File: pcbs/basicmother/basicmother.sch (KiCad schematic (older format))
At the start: 10 parts

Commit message: Primera version de la placa madre y sigo agregando bibliotecas
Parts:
- added C? (x2): 22n, symbol CPSMALL
- added C? (x2): 100n, symbol CPSMALL
- added C? (x2): 100uA, symbol CAPAPOL
- added P?: CONN_3X2, symbol CONN_3X2
- added U?: PTN4050, symbol PTN4050
- added X?: 18.452 MHz, symbol CRYSTAL
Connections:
- net labels added: MISO, MOSI, RST, SCK
- wire segments 66 -> 112
- no-connect marks 27 -> 30
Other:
- note added: "Bajar de 14.8 a 5"
- note added: "Dejando abierto el \npin 3 la salida es 5 V"
- note added: "Elevar de 5 a 12 con PTN04050c"

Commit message: Actualizando la nueva placa base, falta el amplificador para el parlante
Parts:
- removed C? (x2): 22n, symbol CPSMALL
- removed C? (x2): 100n, symbol CPSMALL
- removed C? (x2): 100uA, symbol CAPAPOL
- removed P?: CONN_8, symbol CONN_8
- removed P?: CONN_5X2, symbol CONN_5X2
- removed P? (x4): CONN_2, symbol CONN_2
- removed P?: CONN_3X2, symbol CONN_3X2
- removed U?: PTN4050, symbol PTN4050
- added C? (x2): 22n, symbol Csmall
- added C? (x2): 100n, symbol Csmall
- added P?: CONN_02X03, symbol CONN_02X03
- added P?: CONN_02X05, symbol CONN_02X05
- added P? (x2): CONN_01X02, symbol CONN_01X02
- added P?: CONN_01X08, symbol CONN_01X08
- X?: value 18.452 MHz -> 18.432 MHz
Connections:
- net labels added: +15V
- net labels removed: BAT, POWER
- wire segments 112 -> 114
- no-connect marks 30 -> 28
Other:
- note added: "Comunicacion con el control remoto"
- note added: "Conector para los ojos"
- note added: "Control de los ojos"
- note removed: "Bajar de 14.8 a 5"
- note removed: "CONECTOR DE BATERIA"
- note removed: "CONECTOR DE ENCENDIDO"
- note removed: "Dejando abierto el \npin 3 la salida es 5 V"
- note removed: "Elevar de 5 a 12 con PTN04050c"
- moved on the sheet: IC?, P?, U?, X?

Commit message: actualizo la placa principal
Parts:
- removed P?: CONN_01X08, symbol CONN_01X08
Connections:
- net labels added: Audio
- wire segments 114 -> 123
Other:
- note removed: "CONTRO DE PUENTE H"
- moved on the sheet: P?
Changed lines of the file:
@@
 LIBS:ptn04050c
 LIBS:ptn78000w
+LIBS:drv8432
 LIBS:basicmother-cache
 EELAYER 25 0
@@
 $Descr A4 11693 8268
 encoding utf-8
-Sheet 1 2
+Sheet 1 4
 Title ""
 Date "11 jan 2014"
@@
 Comment4 ""
 $EndDescr
-Text Label 9350 5500 2    60   ~ 0
+Text Label 8000 5700 0    60   ~ 0
 /RESET_CD
-Text Label 9350 5600 2    60   ~ 0
+Text Label 8000 5150 0    60   ~ 0
 PWM_C
-Text Label 9350 5700 2    60   ~ 0
+Text Label 8000 5000 0    60   ~ 0
 PWM_B
-Text Label 9350 5800 2    60   ~ 0
+Text Label 8000 5550 0    60   ~ 0
 /RESET_AB
-Text Label 9350 5900 2    60   ~ 0
+Text Label 8000 4850 0    60   ~ 0
 PWM_A
-Text Label 9350 6000 2    60   ~ 0
+Text Label 8000 5850 0    60   ~ 0
 /FAULT
-Text Label 9350 6100 2    60   ~ 0
+Text Label 8000 6000 0    60   ~ 0
 /OTW
-Text Label 9350 5400 2    60   ~ 0
+Text Label 8000 5300 0    60   ~ 0
 PWM_D
 $Comp
@@
 	3300 5050 3300 4700
 Wire Wire Line
-	1050 5400 1450 5400
+	1050 5400 1200 5400
+Wire Wire Line
+	1200 5400 1450 5400
 $Comp
 L GND #PWR?
@@
 	1000 850  1000 2050
 Wire Notes Line
-	8400 6250 9600 6250
-Wire Notes Line
-	9600 5050 8400 5050
-Wire Notes Line
-	8400 5050 8400 6250
-Wire Notes Line
 	4400 4450 4400 5750
 Wire Notes Line
@@
 Text Notes 1700 1000 0    60   ~ 0
 DIPSWITCH
-Text Notes 9100 5200 0    60   ~ 0
-CONTRO DE PUENTE H
-Wire Notes Line
-	9850 5050 10850 5050
-Wire Notes Line
-	10850 5050 10850 6250
-Wire Notes Line
-	10850 6250 9850 6250
-Wire Wire Line
-	10550 5650 10550 5500
-Wire Wire Line
-	10550 5500 10400 5500
-$Comp
-L GND #PWR?
-U 1 1 52D08C4C
-P 10400 5500
-F 0 "#PWR?" H 10400 5500 30  0001 C CNN
-F 1 "GND" H 10400 5430 30  0001 C CNN
-F 2 "" H 10400 5500 60  0000 C CNN
-F 3 "" H 10400 5500 60  0000 C CNN
-	1    10400 5500
-	0    1    1    0
-$EndComp
-Wire Wire Line
-	10650 5650 10650 5500
-Wire Wire Line
-	10650 5500 10800 5500
-Wire Notes Line
-	9550 5050 9950 5050
-Wire Notes Line
-	9550 6250 10100 6250
-Wire Wire Line
-	9850 5650 9850 5500
-Wire Wire Line
-	9850 5500 9700 5500
-$Comp
-L GND #PWR?
-U 1 1 52D08D21
-P 9700 5500
-F 0 "#PWR?" H 9700 5500 30  0001 C CNN
-F 1 "GND" H 9700 5430 30  0001 C CNN
-F 2 "" H 9700 5500 60  0000 C CNN
-F 3 "" H 9700 5500 60  0000 C CNN
-	1    9700 5500
-	0    1    1    0
-$EndComp
-Wire Wire Line
-	9950 5650 9950 5500
-Wire Wire Line
-	9950 5500 10100 5500
 $Comp
 L +12V #PWR?
 U 1 1 52D08D2C
-P 10100 5450
-F 0 "#PWR?" H 10100 5400 20  0001 C CNN
-F 1 "+12V" H 10100 5550 30  0000 C CNN
-F 2 "" H 10100 5450 60  0000 C CNN
-F 3 "" H 10100 5450 60  0000 C CNN
-	1    10100 5450
+P 10150 4800
+F 0 "#PWR?" H 10150 4750 20  0001 C CNN
+F 1 "+12V" H 10150 4900 30  0000 C CNN
+F 2 "" H 10150 4800 60  0000 C CNN
+F 3 "" H 10150 4800 60  0000 C CNN
+	1    10150 4800
 	1    0    0    -1
 $EndComp
@@
 $EndComp
 Wire Wire Line
-	7000 1950 7150 1950
+	7000 1950 7050 1950
+Wire Wire Line
+	7050 1950 7150 1950
 Wire Wire Line
 	7000 1950 7000 1900
@@
 	7750 1950 7850 1950
 Wire Wire Line
-	7850 1800 7850 2000
+	7850 1800 7850 1950
+Wire Wire Line
+	7850 1950 7850 2000
 Wire Wire Line
 	7850 1800 6700 1800
@@
 	4750 1150 4750 1200
 Wire Wire Line
-	4550 1200 4800 1200
+	4550 1200 4750 1200
+Wire Wire Line
+	4750 1200 4800 1200
 $Comp
 L +5V #PWR?
@@
 	4800 3400 4700 3400
 Wire Wire Line
-	4700 3400 4700 3600
+	4700 3400 4700 3500
+Wire Wire Line
+	4700 3500 4700 3600
 Wire Wire Line
 	4800 3500 4700 3500
@@
 L CONN_01X02 P?
 U 1 1 54D56E87
-P 10600 5850
-F 0 "P?" H 10600 6000 50  0000 C CNN
-F 1 "CONN_01X02" V 10700 5850 50  0000 C CNN
-F 2 "" H 10600 5850 60  0000 C CNN
-F 3 "" H 10600 5850 60  0000 C CNN
-	1    10600 5850
-	0    1    1    0
+P 10350 5550
+F 0 "P?" H 10350 5700 50  0000 C CNN
+F 1 "CONN_01X02" V 10450 5550 50  0000 C CNN
+F 2 "" H 10350 5550 60  0000 C CNN
+F 3 "" H 10350 5550 60  0000 C CNN
+	1    10350 5550
+	1    0    0    -1
 $EndComp
 $Comp
 L CONN_01X02 P?
 U 1 1 54D57006
-P 9900 5850
-F 0 "P?" H 9900 6000 50  0000 C CNN
-F 1 "CONN_01X02" V 10000 5850 50  0000 C CNN
-F 2 "" H 9900 5850 60  0000 C CNN
-F 3 "" H 9900 5850 60  0000 C CNN
-	1    9900 5850
-	0    1    1    0
-$EndComp
-$Comp
-L CONN_01X08 P?
-U 1 1 54D5705C
-P 8600 5750
-F 0 "P?" H 8600 6200 50  0000 C CNN
-F 1 "CONN_01X08" V 8700 5750 50  0000 C CNN
-F 2 "" H 8600 5750 60  0000 C CNN
-F 3 "" H 8600 5750 60  0000 C CNN
-	1    8600 5750
-	-1   0    0    -1
-$EndComp
-Wire Wire Line
-	9350 6100 8800 6100
-Wire Wire Line
-	8800 6000 9350 6000
-Wire Wire Line
-	9350 5900 8800 5900
-Wire Wire Line
-	8800 5800 9350 5800
-Wire Wire Line
-	9350 5700 8800 5700
-Wire Wire Line
-	8800 5600 9350 5600
-Wire Wire Line
-	9350 5500 8800 5500
-Wire Wire Line
-	8800 5400 9350 5400
+P 10350 5250
+F 0 "P?" H 10350 5400 50  0000 C CNN
+F 1 "CONN_01X02" V 10450 5250 50  0000 C CNN
+F 2 "" H 10350 5250 60  0000 C CNN
+F 3 "" H 10350 5250 60  0000 C CNN
+	1    10350 5250
+	1    0    0    -1
+$EndComp
+Wire Wire Line
+	8000 6000 8550 6000
+Wire Wire Line
+	8550 5850 8000 5850
+Wire Wire Line
+	8000 4850 8550 4850
+Wire Wire Line
+	8550 5550 8000 5550
+Wire Wire Line
+	8000 5000 8550 5000
+Wire Wire Line
+	8550 5150 8000 5150
+Wire Wire Line
+	8000 5700 8550 5700
+Wire Wire Line
+	8550 5300 8000 5300
 $Sheet
 S 10200 950  750  1000
@@
 L +15V #PWR?
 U 1 1 54D5DC54
-P 10800 5450
-F 0 "#PWR?" H 10800 5300 60  0001 C CNN
-F 1 "+15V" H 10800 5590 60  0000 C CNN
-F 2 "" H 10800 5450 60  0000 C CNN
-F 3 "" H 10800 5450 60  0000 C CNN
-	1    10800 5450
-	1    0    0    -1
-$EndComp
-Wire Wire Line
-	10800 5500 10800 5450
-Wire Wire Line
-	10100 5500 10100 5450
+P 9950 4700
+F 0 "#PWR?" H 9950 4550 60  0001 C CNN
+F 1 "+15V" H 9950 4840 60  0000 C CNN
+F 2 "" H 9950 4700 60  0000 C CNN
+F 3 "" H 9950 4700 60  0000 C CNN
+	1    9950 4700
+	1    0    0    -1
+$EndComp
+$Comp
+L +15V #PWR?
+U 1 1 54DE957E
+P 9750 900
+F 0 "#PWR?" H 9750 750 60  0001 C CNN
+F 1 "+15V" H 9750 1040 60  0000 C CNN
+F 2 "" H 9750 900 60  0000 C CNN
+F 3 "" H 9750 900 60  0000 C CNN
+	1    9750 900
+	1    0    0    -1
+$EndComp
+$Sheet
+S 9500 2500 1100 950
+U 54DEA09E
+F0 "sound" 60
+F1 "sound.sch" 60
+F2 "In" I L 9500 3000 60
+F3 "5V" I L 9500 2700 60
+F4 "GND" I L 9500 3250 60
+$EndSheet
+Wire Wire Line
+	9500 2700 9300 2700
+Wire Wire Line
+	9300 2700 9300 2300
+$Comp
+L +5V #PWR?
+U 1 1 54DEDB40
+P 9300 2300
+F 0 "#PWR?" H 9300 2390 20  0001 C CNN
+F 1 "+5V" H 9300 2390 30  0000 C CNN
+F 2 "" H 9300 2300 60  0000 C CNN
+F 3 "" H 9300 2300 60  0000 C CNN
+	1    9300 2300
+	1    0    0    -1
+$EndComp
+$Comp
+L GND #PWR?
+U 1 1 54DEDBE5
+P 9300 3350
+F 0 "#PWR?" H 9300 3350 30  0001 C CNN
+F 1 "GND" H 9300 3280 30  0001 C CNN
+F 2 "" H 9300 3350 60  0000 C CNN
+F 3 "" H 9300 3350 60  0000 C CNN
+	1    9300 3350
+	1    0    0    -1
+$EndComp
+Wire Wire Line
+	9300 3350 9300 3250
+Wire Wire Line
+	9300 3250 9500 3250
+Wire Wire Line
+	9500 3000 9150 3000
+Text Label 9150 3000 0    60   ~ 0
+Audio
+Text Label 3750 7300 2    60   ~ 0
+Audio
+Wire Wire Line
+	3750 7300 3300 7300
+$Sheet
+S 8550 4700 1250 1450
+U 54DEEEE7
+F0 "motordrv" 60
+F1 "motordrv.sch" 60
+F2 "MOUT_D" U R 9800 5600 60
+F3 "MOUT_C" U R 9800 5500 60
+F4 "MOUT_B" U R 9800 5300 60
+F5 "MOUT_A" U R 9800 5200 60
+F6 "~RESET_AB" I L 8550 5550 60
+F7 "~RESET_CD" I L 8550 5700 60
+F8 "PWM_D" I L 8550 5300 60
+F9 "PWM_C" I L 8550 5150 60
+F10 "PWM_B" I L 8550 5000 60
+F11 "PWM_A" I L 8550 4850 60
+F12 "PVDD" I R 9800 4850 60
+F13 "~FAULT" O L 8550 5850 60
+F14 "~OTW" O L 8550 6000 60
+F15 "DGND" I R 9800 5850 60
+F16 "DVDD" I R 9800 5000 60
+$EndSheet
+Wire Wire Line
+	9950 4700 9950 4850
+Wire Wire Line
+	9950 4850 9800 4850
+Wire Wire Line
+	10150 4800 10150 5000
+Wire Wire Line
+	10150 5000 9800 5000
+Wire Wire Line
+	10150 5500 9800 5500
+Wire Wire Line
+	9800 5600 10150 5600
+Wire Wire Line
+	10150 5300 9800 5300
+Wire Wire Line
+	9800 5200 10150 5200
 $EndSCHEMATC

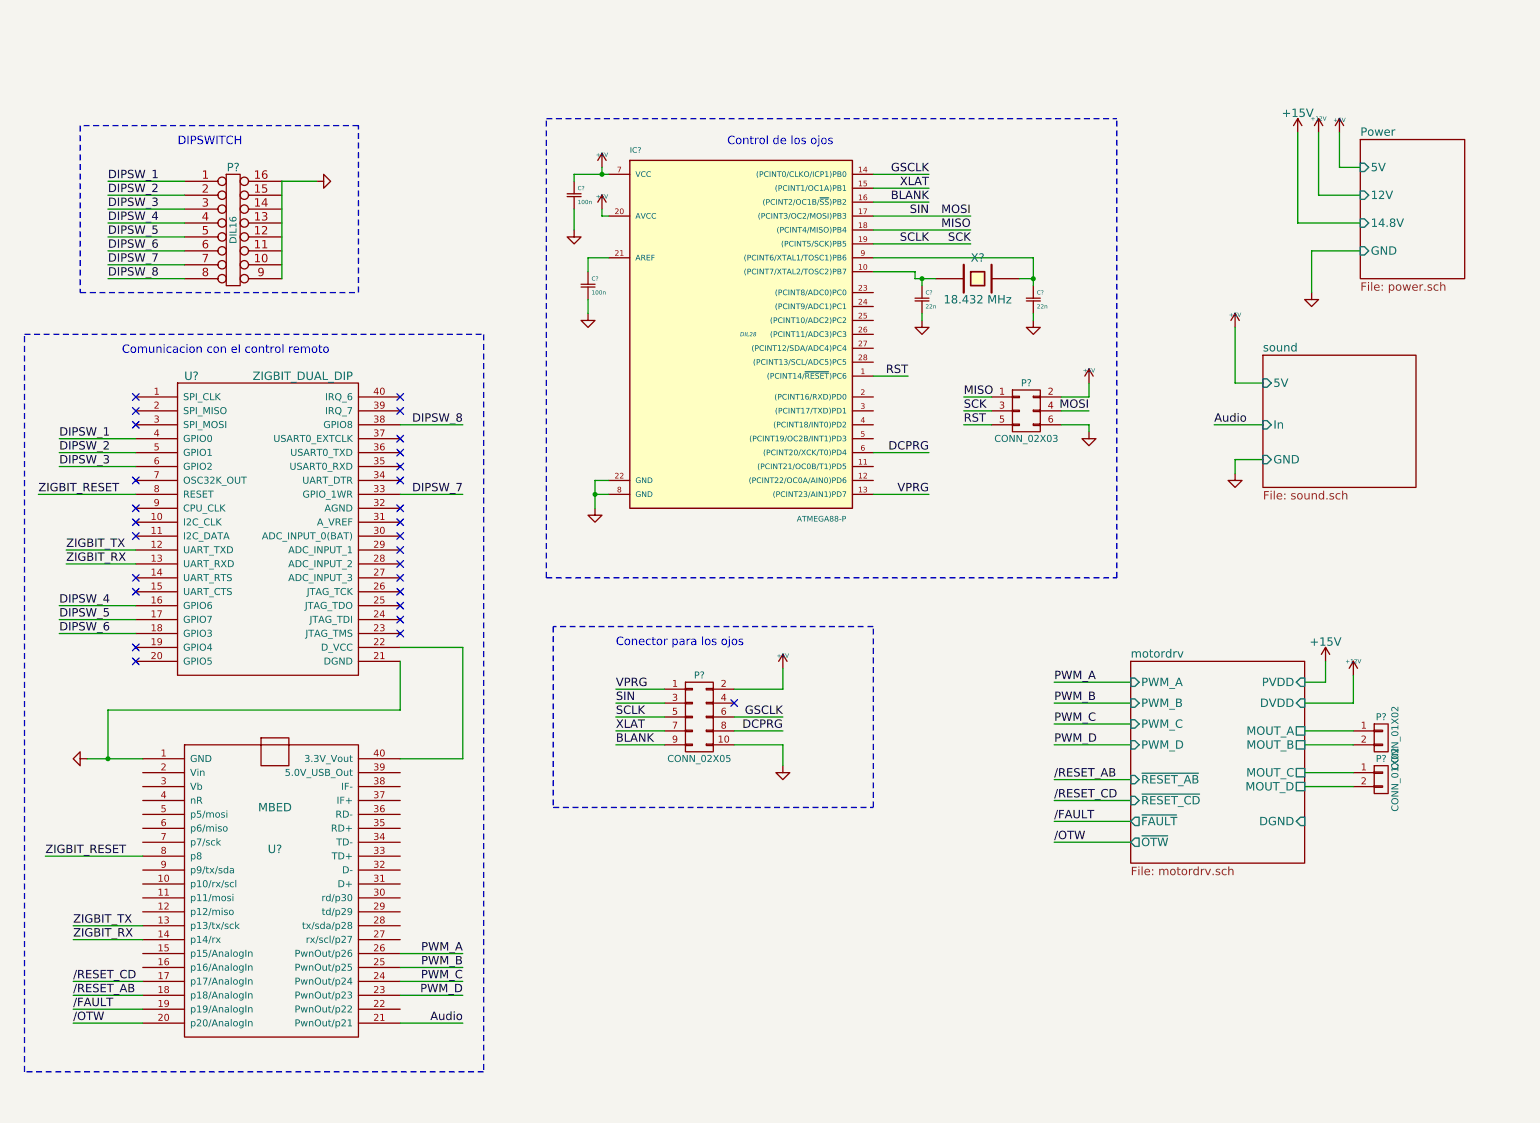
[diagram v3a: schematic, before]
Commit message: Actualizo esquematico de la placa principal y empiezo con el layout
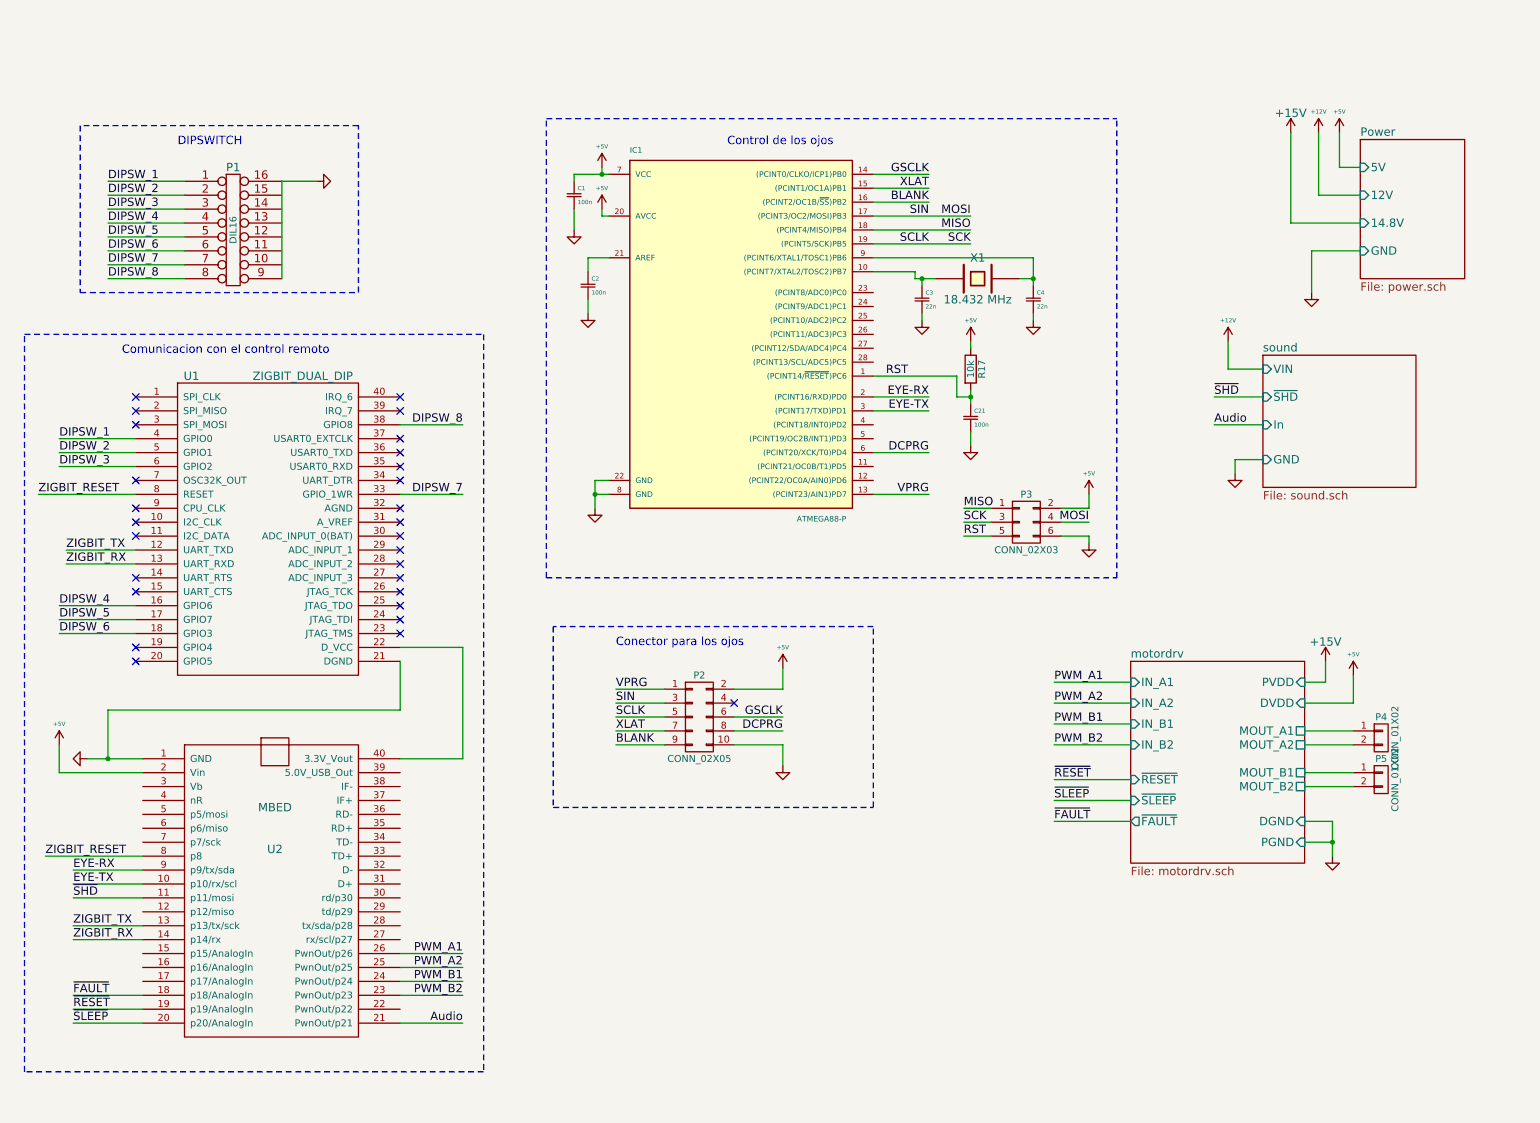
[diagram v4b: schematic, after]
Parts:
- added C21: 100n, Capacitors_ThroughHole:C_Disc_D3_P2.5, symbol Csmall
- added R17: 10k, Resistors_ThroughHole:Resistor_Horizontal_RM10mm, symbol R
- C1, C2, C3, C4: renamed from C?; footprint (none) -> Capacitors_ThroughHole:C_Disc_D3_P2.5
- IC1: renamed from IC?; footprint DIL28 -> Sockets_DIP:DIP-28__300
- P1: renamed from P?; footprint (none) -> Sockets_DIP:DIP-16__300
- P2: renamed from P?; footprint (none) -> Pin_Headers:Pin_Header_Straight_2x05
- P3: renamed from P?; footprint (none) -> Pin_Headers:Pin_Header_Straight_2x03
- P4, P5: renamed from P?; footprint (none) -> Pin_Headers:Pin_Header_Straight_1x02
- U1: renamed from U?; footprint (none) -> Popurri_CDR:ZIGBIT_DIP_40
- U2: renamed from U?; footprint (none) -> Popurri_CDR:MBED
- X1: renamed from X?; footprint (none) -> Crystals:Crystal_HC49-U_Vertical
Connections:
- net +5V: now also U2.2 (Vin), R17.1
- net GND: now also C21.2
- net RST: now also C21.1, R17.2
- net EYE-TX: now reaches U2.10 (p10/rx/scl)
- net EYE-TX: now also IC1.3 ((PCINT17/TXD)PD1)
- net ~SHD: now reaches U2.11 (p11/mosi)
- net EYE-RX: now reaches U2.9 (p9/tx/sda)
- net EYE-RX: now also IC1.2 ((PCINT16/RXD)PD0)
- net /FAULT renamed ~RESET
- net /OTW renamed ~SLEEP
- net /RESET_AB renamed ~FAULT
- net /RESET_CD: no longer names the net of U2.17 (p17/AnalogIn)
- net PWM_A renamed PWM_A1
- net PWM_B renamed PWM_A2
- net PWM_C renamed PWM_B1
- net PWM_D renamed PWM_B2
- net motordrv/MOUT_A renamed motordrv/MOUT_A1
- net motordrv/MOUT_B renamed motordrv/MOUT_A2
- net motordrv/MOUT_C renamed motordrv/MOUT_B1
- net motordrv/MOUT_D renamed motordrv/MOUT_B2
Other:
- moved on the sheet: P3

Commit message: agrego algunos cambios en el control y casi termino la placa principal
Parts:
- added D?: LED, symbol LED
- added R?: R, symbol R
- added U?: bluetooth-mod, symbol bluetooth-mod
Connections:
- net GND: now also D?.2 (K), U?.13 (GND), U?.22 (GND)
- net MIC: now reaches U2.15 (p15/AnalogIn)
- net +3V3: now reaches U1.22 (D_VCC), U2.40 (3.3V_Vout)
- net +3V3: now also U?.12 (3.3V)
- new net: R?.1, U?.24 (LED)
- new net: D?.1 (A), R?.2
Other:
- moved on the sheet: P2, P4, P5

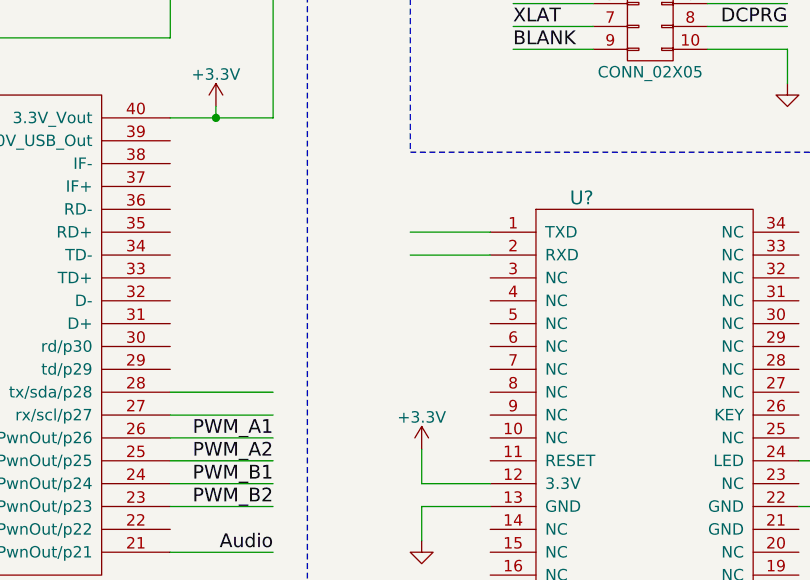
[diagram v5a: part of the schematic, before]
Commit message: completo el esquematico del control y asigno footprints
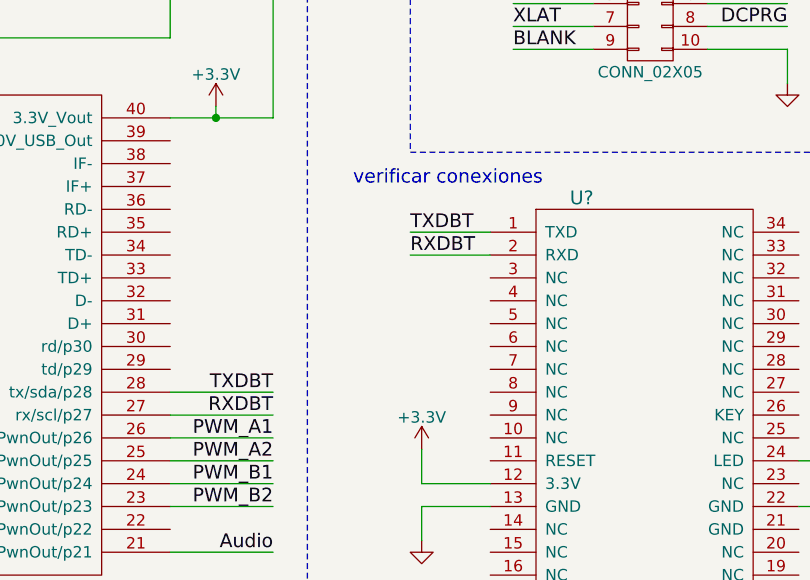
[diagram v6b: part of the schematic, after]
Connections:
- net RXDBT: now reaches U2.27 (rx/scl/p27)
- net RXDBT: now also U?.2 (RXD)
- net TXDBT: now reaches U2.28 (tx/sda/p28)
- net TXDBT: now also U?.1 (TXD)
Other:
- note added: "verificar conexiones"
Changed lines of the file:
@@
 LIBS:ptn78000w
 LIBS:drv8432
-LIBS:lm4950
 LIBS:drv8843
 LIBS:lmz12002
@@
 	1    0    0    -1
 $EndComp
+Text Label 4350 5900 0    60   ~ 0
+TXDBT
+Text Label 4350 6000 0    60   ~ 0
+RXDBT
+Text Label 3750 6700 2    60   ~ 0
+RXDBT
+Text Label 3750 6600 2    60   ~ 0
+TXDBT
+Text Notes 4100 5700 0    60   ~ 0
+verificar conexiones
 $EndSCHEMATC
